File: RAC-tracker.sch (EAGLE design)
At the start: 26 parts, among them J1 U.FL, J2 U.FL, J5 CORTEX_JTAG_DEBUG_MINIMUM_SMD, U1 NRF9160-SICA-R, U2 SIM-ST-MFF2, U3 MCP73831, U4 SKY65723-81, U5 MIC5365-1.8YC5-TR

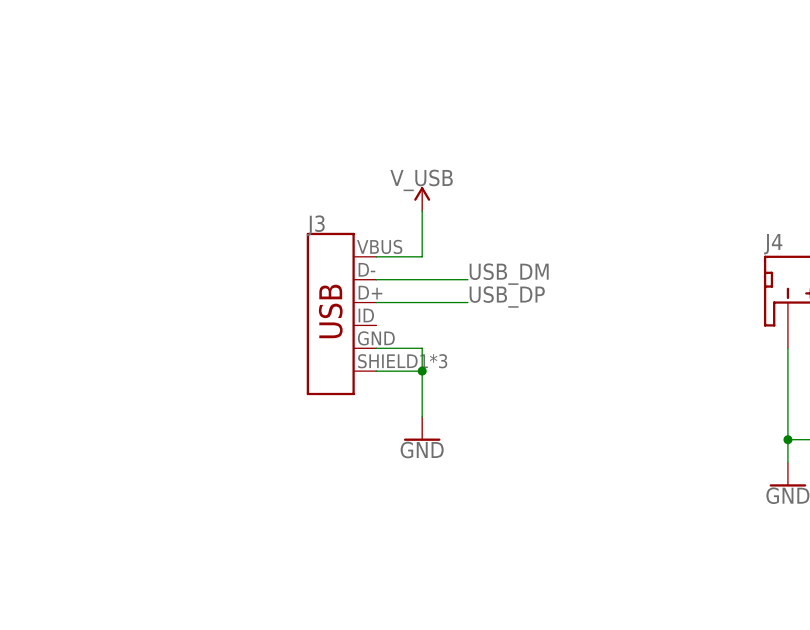
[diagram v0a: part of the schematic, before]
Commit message: Added a purchasable Molex Micro-USB connector
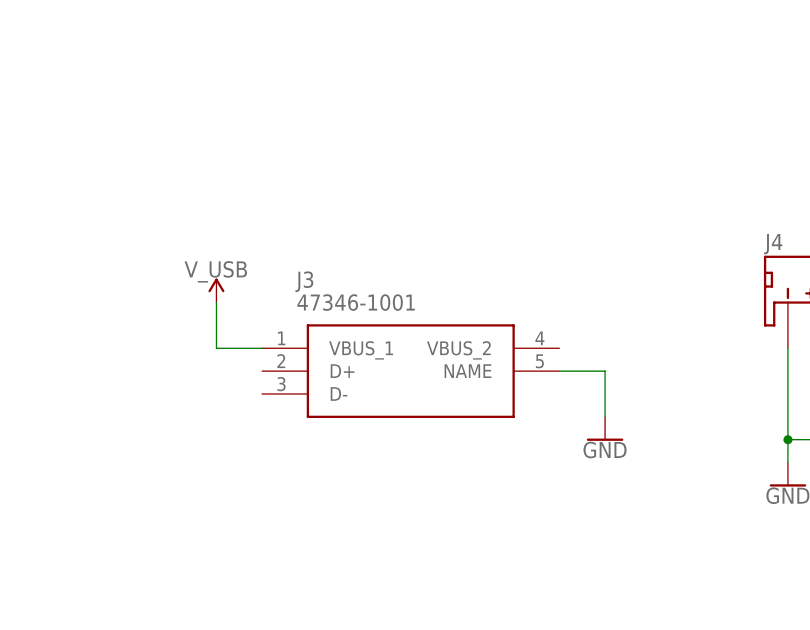
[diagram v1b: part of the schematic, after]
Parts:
- J3: value (none) -> 47346-1001; device SparkFun-Connectors:USB_MICRO-B_FEMALE-SMT -> rocket-components:47346-1001
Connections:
- removed net USB_DM: J3.D-
- removed net USB_DP: J3.D+
- net GND: now also J3.NAME; no longer J3.GND, J3.SHIELD
- net V_USB: now also J3.VBUS_1; no longer J3.VBUS
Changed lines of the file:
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@@
 <part name="C5" library="SparkFun-Capacitors" library_urn="urn:adsk.eagle:library:510" deviceset="0.1UF" device="-0603-25V-(+80/-20%)" package3d_urn="urn:adsk.eagle:package:37414/1" value="0.1uF"/>
 <part name="GND1" library="SparkFun-PowerSymbols" library_urn="urn:adsk.eagle:library:530" deviceset="GND" device=""/>
-<part name="J3" library="SparkFun-Connectors" deviceset="USB_MICRO-B" device="_FEMALE-SMT"/>
-<part name="SUPPLY4" library="SparkFun-PowerSymbols" library_urn="urn:adsk.eagle:library:530" deviceset="V_USB" device=""/>
-<part name="GND9" library="SparkFun-PowerSymbols" library_urn="urn:adsk.eagle:library:530" deviceset="GND" device=""/>
 <part name="U3" library="SparkFun-IC-Power" deviceset="MCP73831" device=""/>
 <part name="SUPPLY6" library="SparkFun-PowerSymbols" library_urn="urn:adsk.eagle:library:530" deviceset="V_USB" device=""/>
@@
 <part name="SUPPLY2" library="SparkFun-PowerSymbols" library_urn="urn:adsk.eagle:library:530" deviceset="1.8V" device=""/>
 <part name="GND19" library="SparkFun-PowerSymbols" library_urn="urn:adsk.eagle:library:530" deviceset="GND" device=""/>
+<part name="J3" library="rocket-components" deviceset="47346-1001" device=""/>
+<part name="SUPPLY3" library="SparkFun-PowerSymbols" library_urn="urn:adsk.eagle:library:530" deviceset="V_USB" device=""/>
+<part name="GND20" library="SparkFun-PowerSymbols" library_urn="urn:adsk.eagle:library:530" deviceset="GND" device=""/>
 </parts>
 <sheets>
@@
 <attribute name="VALUE" x="-20.32" y="-45.974" size="1.778" layer="96" align="top-center"/>
 </instance>
-<instance part="J3" gate="J1" x="165.1" y="12.7" smashed="yes">
-<attribute name="VALUE" x="162.56" y="2.794" size="1.778" layer="96" font="vector" rot="MR180" align="top-left"/>
-<attribute name="NAME" x="162.56" y="23.114" size="1.778" layer="95" font="vector"/>
-</instance>
-<instance part="SUPPLY4" gate="G$1" x="175.26" y="25.4" smashed="yes">
-<attribute name="VALUE" x="175.26" y="28.194" size="1.778" layer="96" align="bottom-center"/>
-</instance>
-<instance part="GND9" gate="1" x="175.26" y="0" smashed="yes">
-<attribute name="VALUE" x="175.26" y="-0.254" size="1.778" layer="96" align="top-center"/>
-</instance>
 <instance part="U3" gate="G$1" x="193.04" y="-38.1" smashed="yes">
 <attribute name="NAME" x="185.42" y="-32.512" size="1.778" layer="95"/>
@@
 <instance part="GND19" gate="1" x="-81.28" y="0" smashed="yes">
 <attribute name="VALUE" x="-81.28" y="-0.254" size="1.778" layer="96" align="top-center"/>
+</instance>
+<instance part="J3" gate="G$1" x="157.48" y="10.16" smashed="yes">
+<attribute name="NAME" x="161.29" y="17.78" size="1.778" layer="95" align="center-left"/>
+<attribute name="VALUE" x="161.29" y="15.24" size="1.778" layer="96" align="center-left"/>
+</instance>
+<instance part="SUPPLY3" gate="G$1" x="152.4" y="15.24" smashed="yes">
+<attribute name="VALUE" x="152.4" y="18.034" size="1.778" layer="96" align="bottom-center"/>
+</instance>
+<instance part="GND20" gate="1" x="195.58" y="0" smashed="yes">
+<attribute name="VALUE" x="195.58" y="-0.254" size="1.778" layer="96" align="top-center"/>
 </instance>
 </instances>
@@
 <wire x1="-25.4" y1="-35.56" x2="-20.32" y2="-35.56" width="0.1524" layer="91"/>
 <junction x="-20.32" y="-35.56"/>
-</segment>
-<segment>
-<pinref part="J3" gate="J1" pin="SHIELD"/>
-<wire x1="170.18" y1="7.62" x2="175.26" y2="7.62" width="0.1524" layer="91"/>
-<pinref part="GND9" gate="1" pin="GND"/>
-<wire x1="175.26" y1="7.62" x2="175.26" y2="2.54" width="0.1524" layer="91"/>
-<pinref part="J3" gate="J1" pin="GND"/>
-<wire x1="170.18" y1="10.16" x2="175.26" y2="10.16" width="0.1524" layer="91"/>
-<wire x1="175.26" y1="10.16" x2="175.26" y2="7.62" width="0.1524" layer="91"/>
-<junction x="175.26" y="7.62"/>
 </segment>
 <segment>
@@
 <wire x1="-81.28" y1="7.62" x2="-76.2" y2="7.62" width="0.1524" layer="91"/>
 </segment>
+<segment>
+<pinref part="J3" gate="G$1" pin="NAME"/>
+<wire x1="190.5" y1="7.62" x2="195.58" y2="7.62" width="0.1524" layer="91"/>
+<wire x1="195.58" y1="7.62" x2="195.58" y2="2.54" width="0.1524" layer="91"/>
+<pinref part="GND20" gate="1" pin="GND"/>
+</segment>
 </net>
 <net name="SIM_VIN" class="0">
@@
 <net name="V_USB" class="0">
 <segment>
-<pinref part="J3" gate="J1" pin="VBUS"/>
-<wire x1="170.18" y1="20.32" x2="175.26" y2="20.32" width="0.1524" layer="91"/>
-<pinref part="SUPPLY4" gate="G$1" pin="V_USB"/>
-<wire x1="175.26" y1="20.32" x2="175.26" y2="25.4" width="0.1524" layer="91"/>
-</segment>
-<segment>
 <pinref part="R2" gate="G$1" pin="2"/>
 <wire x1="167.64" y1="-40.64" x2="167.64" y2="-35.56" width="0.1524" layer="91"/>
@@
 <junction x="157.48" y="-35.56"/>
 </segment>
-</net>
-<net name="USB_DM" class="0">
-<segment>
-<pinref part="J3" gate="J1" pin="D-"/>
-<wire x1="170.18" y1="17.78" x2="180.34" y2="17.78" width="0.1524" layer="91"/>
-<label x="180.34" y="17.78" size="1.778" layer="95"/>
-</segment>
-</net>
-<net name="USB_DP" class="0">
-<segment>
-<pinref part="J3" gate="J1" pin="D+"/>
-<wire x1="170.18" y1="15.24" x2="180.34" y2="15.24" width="0.1524" layer="91"/>
-<label x="180.34" y="15.24" size="1.778" layer="95"/>
-</segment>
-</net>
+<segment>
+<pinref part="J3" gate="G$1" pin="VBUS_1"/>
+<wire x1="157.48" y1="10.16" x2="152.4" y2="10.16" width="0.1524" layer="91"/>
+<wire x1="152.4" y1="10.16" x2="152.4" y2="15.24" width="0.1524" layer="91"/>
+<pinref part="SUPPLY3" gate="G$1" pin="V_USB"/>
+</segment>
+</net>

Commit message: U.FL replaced to fit BOM, polygons adjusted. Fab ready!
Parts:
- C1: value 4.7uF -> 56pF; device SparkFun-Capacitors:4.7UF0603 -> rocket-components:GRM1885C1H560JA01J
- C10: value 1.0uF -> 47uF; device SparkFun-Capacitors:1.0UF-0603-16V-10% -> rocket-components:JMK212BBJ476MG-T
- C2: value 4.7uF -> 0.1uF; device SparkFun-Capacitors:4.7UF0603 -> SparkFun-Capacitors:0.1UF-0603-25V-(+80/-20%)
- C3: value 4.7uF -> 1.0uF; device SparkFun-Capacitors:4.7UF0603 -> SparkFun-Capacitors:1.0UF-0603-16V-10%
- C4: value 47uF -> 1.0uF; device rocket-components:JMK212BBJ476MG-T -> SparkFun-Capacitors:1.0UF-0603-16V-10%
- C5: value 0.1uF -> 4.7uF; device SparkFun-Capacitors:0.1UF-0603-25V-(+80/-20%) -> SparkFun-Capacitors:4.7UF0603
- C8: value 56pF -> 4.7uF; device rocket-components:GRM1885C1H560JA01J -> SparkFun-Capacitors:4.7UF0603
- C9: value 1.0uF -> 4.7uF; device SparkFun-Capacitors:1.0UF-0603-16V-10% -> SparkFun-Capacitors:4.7UF0603
- J1, J2: value U.FL -> 2337019-1; device SparkFun-Connectors:U.FL -> rocket-components:2337019-1
- R1: value 2.0k -> 1k; device SparkFun-Resistors:2.0KOHM-0603-1/10W-5% -> SparkFun-Resistors:1KOHM-0603-1/10W-1%
- R2: value 1k -> 2.0k; device SparkFun-Resistors:1KOHM-0603-1/10W-1% -> SparkFun-Resistors:2.0KOHM-0603-1/10W-5%
- renumbered D3 to D2
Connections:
- net 1.8V: now also C1.1, C4.1, C7.1; no longer C10.1, C3.1, C8.1
- net GND: now also J1.GND_1, J1.GND_2, J2.GND_1, J2.GND_2, R2.1; no longer J1.GND@0, J1.GND@1, J2.GND@0, J2.GND@1, R1.1
- net IO_SUP: now also C10.1; no longer C4.1
- net PROG: now also R2.2; no longer R1.2
- net SIM_VIN: now also C2.1; no longer C5.1
- net STAT_AN: now also R1.1; no longer R2.1
- net V_BATT: now also C3.1, C5.1, C6.1; no longer C1.1, C2.1, C7.1
- net V_USB: now also C8.1, R1.2; no longer C6.1, R2.2
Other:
- moved on the sheet: C2, C3, C5, C6, C7, C9, R1, R2

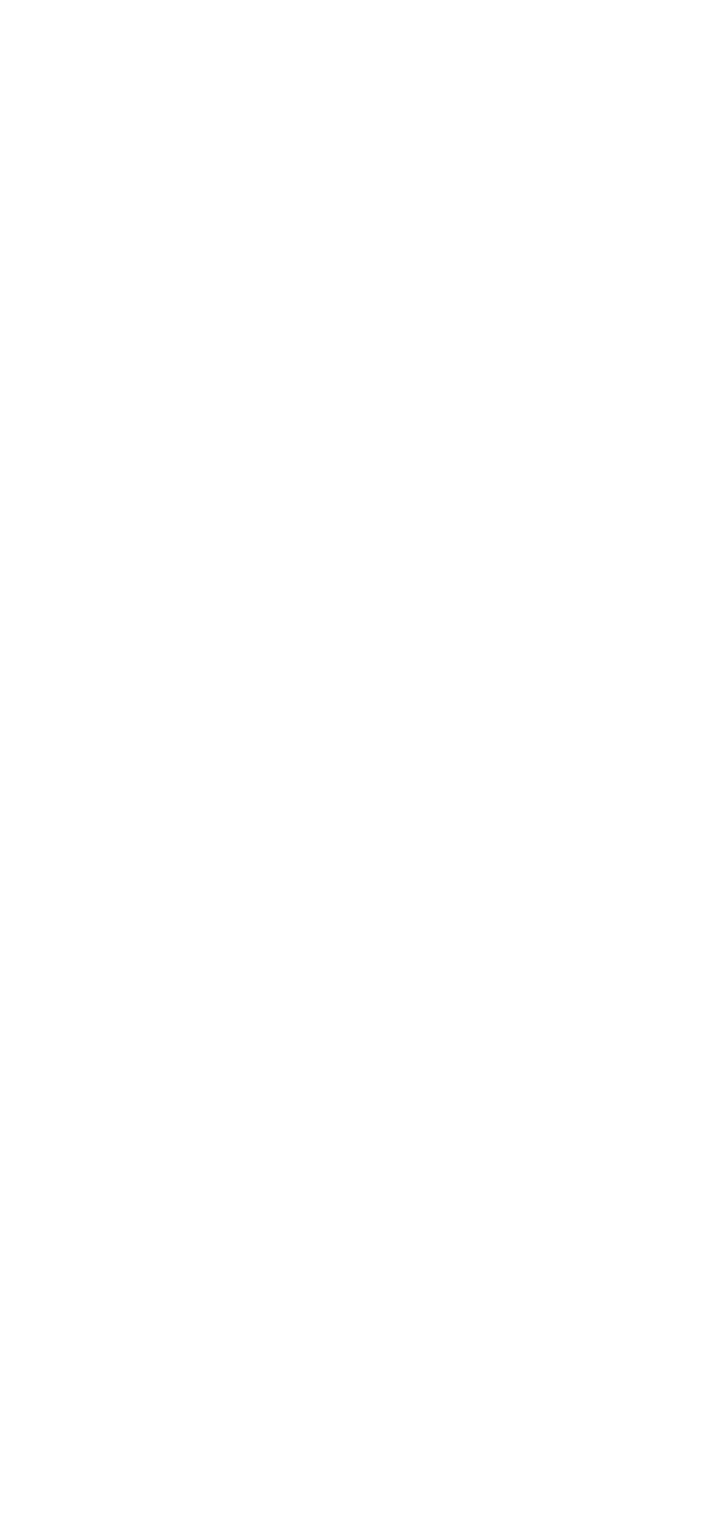
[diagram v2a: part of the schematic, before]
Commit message: Starting again with the SIM7000
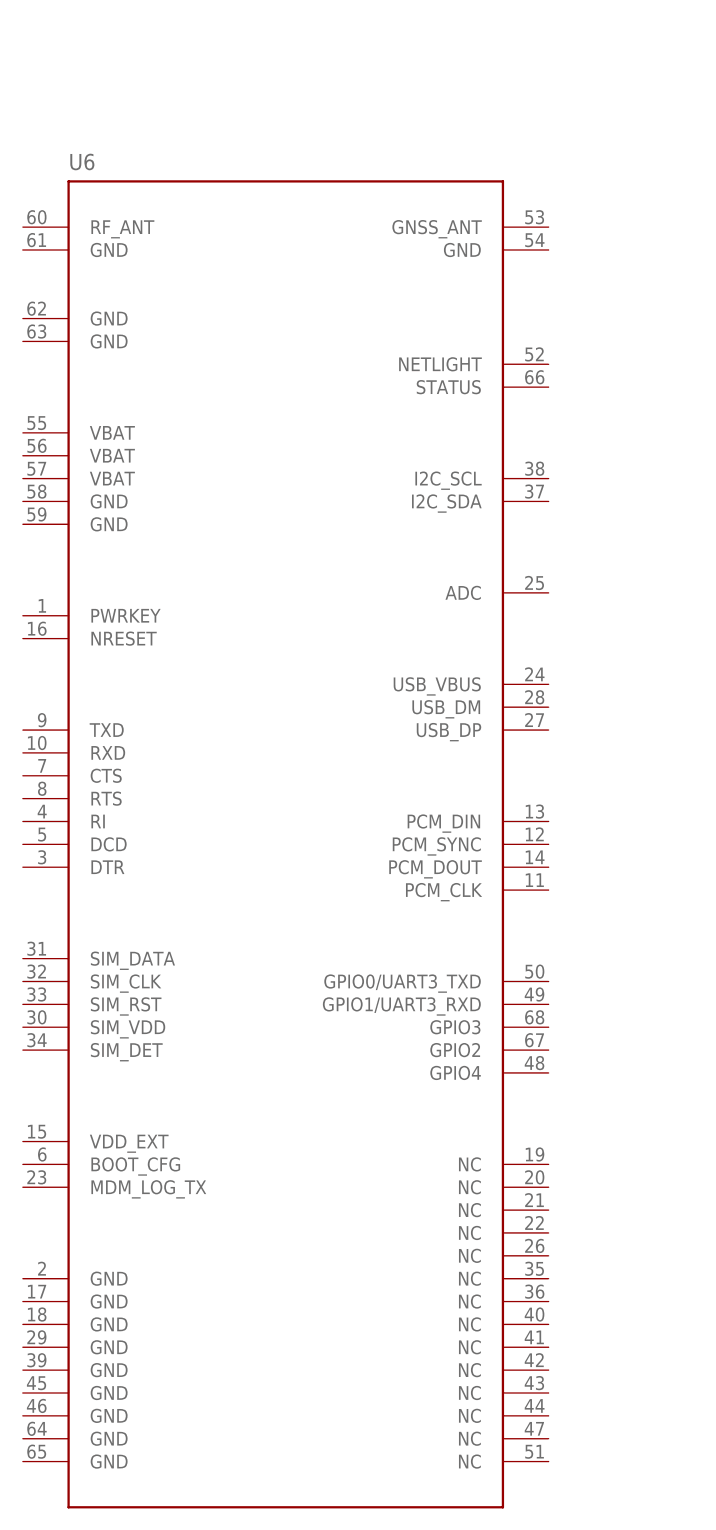
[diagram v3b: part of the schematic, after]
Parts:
- added U6: (no value), rocket-components:SIM7000
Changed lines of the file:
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@@
 <part name="GND9" library="SparkFun-PowerSymbols" library_urn="urn:adsk.eagle:library:530" deviceset="GND" device=""/>
 <part name="GND21" library="SparkFun-PowerSymbols" library_urn="urn:adsk.eagle:library:530" deviceset="GND" device=""/>
+<part name="U6" library="rocket-components" deviceset="SIM7000" device=""/>
 </parts>
 <sheets>
@@
 <attribute name="VALUE" x="-71.12" y="45.466" size="1.778" layer="96" align="top-center"/>
 </instance>
+<instance part="U6" gate="G$1" x="-200.66" y="-60.96" smashed="yes">
+<attribute name="NAME" x="-200.66" y="87.63" size="1.778" layer="95"/>
+<attribute name="VALUE" x="-185.42" y="43.18" size="3.81" layer="96"/>
+</instance>
 </instances>

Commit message: Set up minimum schematic for SIM7000
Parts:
- removed C10: 47uF, rocket-components:JMK212BBJ476MG-T
- removed C3, C4: 1.0uF, SparkFun-Capacitors:1.0UF-0603-16V-10%
- removed C5, C6, C7: 4.7uF, SparkFun-Capacitors:4.7UF0603
- removed J5: CORTEX_JTAG_DEBUG_MINIMUM_SMD, SparkFun-Connectors:CORTEX_JTAG_DEBUG_MINIMUM_SMD
- removed R3: 10k, SparkFun-Resistors:10KOHM-0603-1/10W-1%
- removed R4: 1M, SparkFun-Resistors:1MOHM-0603-1/4W-5%
- removed U1: NRF9160-SICA-R, rocket-components:NRF9160-SICA-R
- removed U5: MIC5365-1.8YC5-TR, rocket-components:MIC5365-1.8YC5-TR
- added C11: 0.1uF, SparkFun-Capacitors:0.1UF-0603-25V-(+80/-20%)
- added C12: 1.0uF, SparkFun-Capacitors:1.0UF-0603-16V-10%
- added C13, C14, C15: 100uF, rocket-components:JMK316ABJ107ML-T
- added D3, D4: 250mA/100V, SparkFun-DiscreteSemi:DIODE-BAS16J
- added FB1: 30Ω/1.8A, SparkFun-Coils:FERRITE_BEAD-0603
- added S1: MOMENTARY-SWITCH-SPST-SMD-5.2MM, SparkFun-Switches:MOMENTARY-SWITCH-SPST-SMD-5.2MM
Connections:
- removed net !RST: J5.!RESET, U1.NRESET
- removed net EN: R3.1, U1.ENABLE
- removed net GPS_EN: R4.2, U1.MAGPIO0, U4.VEN
- removed net IO_SUP: C10.1, U1.IO_SUPPLY
- removed net SWDCLK: J5.SWDCLK, U1.SWDCLK
- removed net SWDIO: J5.SWDIO, U1.SWDIO
- new net !LTE_RST: D4.C
- new net DTR: U6.DTR
- new net LTE_PWR: D3.C, S1.2
- new net NRESET: D4.A, U6.NRESET
- new net PWRKEY: D3.A, U6.PWRKEY
- new net RI: U6.RI
- new net RXD: U6.RXD
- new net TXD: U6.TXD
- new net USB_DM: J3.D-, U6.USB_DM
- new net USB_DP: J3.D+, U6.USB_DP
- new net VCC: C11.1, C12.1, C13.1, C14.1, C15.1, FB1.2, U6.VBAT, U6.VBAT@1, U6.VBAT@2
- net 1.8V: now also U4.VEN, U6.VDD_EXT; no longer C4.1, C7.1, J5.VCC, U1.VDD_GPIO, U5.VOUT
- net GND: now also C11.2, C12.2, C13.2, C14.2, C15.2, S1.1, U6.GND, U6.GND@1, U6.GND@10, U6.GND@11, U6.GND@12, U6.GND@13, U6.GND@14, U6.GND@2, U6.GND@3, U6.GND@4, U6.GND@5, U6.GND@6, U6.GND@7, U6.GND@8, U6.GND@9; no longer C10.2, C3.2, C4.2, C5.2, C6.2, C7.2, J5.GND, R4.1, U1.GND_SHIELD, U1.VSS, U5.GND
- net GPS_RF: now also U6.GNSS_ANT; no longer U1.GPS
- net LTE_ANT: now also U6.RF_ANT; no longer U1.ANT
- net SIM_CLK: now also U6.SIM_CLK; no longer U1.SIM_CLK
- net SIM_DATA: now also U6.SIM_DATA; no longer U1.SIM_IO
- net SIM_RST: now also U6.SIM_RST; no longer U1.SIM_RST
- net SIM_VIN: now also U6.SIM_VDD; no longer U1.SIM_1V8
- net V_BATT: now also FB1.1; no longer C3.1, C5.1, C6.1, R3.2, U1.VDD, U5.EN, U5.VIN
- net V_USB: now also U6.USB_VBUS
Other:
- moved on the sheet: C2, J1, J2, U2, U6

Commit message: Replaced u.FL connectors with SMD antennas
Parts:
- removed J1, J2: 2337019-1, rocket-components:2337019-1
- removed S1: MOMENTARY-SWITCH-SPST-SMD-5.2MM, SparkFun-Switches:MOMENTARY-SWITCH-SPST-SMD-5.2MM
- added AE1: FR01-S4-232L, rocket-components:FR01-S4-232L
- added AE2: W3011, rocket-components:W3011
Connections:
- net USB_DM renamed USB_N
- net USB_DP renamed USB_P
- net GND: now also AE2.GND; no longer J1.GND_1, J1.GND_2, J2.GND_1, J2.GND_2, S1.1
- net GPS_ANT: now also AE2.FEED; no longer J1.SIGNAL
- net LTE_ANT: now also AE1.SIGNAL; no longer J2.SIGNAL
- net LTE_PWR: no longer S1.2
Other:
- moved on the sheet: C1, C2, C8, C9, D1, D2, J3, J4, R1, R2, U2, U3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

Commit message: Added ATMEGA328P and BMP388 to schematic, likely won't keep
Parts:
- removed D3, D4: 250mA/100V, SparkFun-DiscreteSemi:DIODE-BAS16J
- added C3, C5: 0.1uF, SparkFun-Capacitors:0.1UF-0603-25V-(+80/-20%)
- added C4: 4.7uF, SparkFun-Capacitors:4.7UF0603
- added D5: BLUE, SparkFun-LED:LED-BLUE0603
- added D6: GREEN, SparkFun-LED:LED-GREEN0603
- added JP1: (no value), pinhead:PINHD-1X6
- added Q1, Q2: 220mA/50V/3.5Ω, SparkFun-DiscreteSemi:MOSFET-NCH-BSS138
- added R3: 2.0k, SparkFun-Resistors:2.0KOHM-0603-1/10W-5%
- added R4: 470, SparkFun-Resistors:470OHM-0603-1/10W-1%
- added R5, R6: 4.7k, SparkFun-Resistors:4.7KOHM-0603-1/10W-1%
- added U1: ATMEGA328P, SparkFun-IC-Microcontroller:ATMEGA328P_VQFNVQFN
- added U5: BMP388, SparkFun-Sensors:BMP388BMP388
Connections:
- removed net !LTE_RST: D4.C
- removed net LTE_PWR: D3.C
- removed net RXD: U6.RXD
- removed net TXD: U6.TXD
- new net LED_NET_A: D5.A, R4.1
- new net LED_NET_C: D5.C, Q2.D
- new net LED_STAT_A: D6.A, R3.1
- new net LED_STAT_C: D6.C, Q1.D
- new net LTE_RXD: U1.PD1(TXD), U6.RXD
- new net LTE_TXD: U1.PD0(RXD), U6.TXD
- new net MCU_RST: JP1.3, U1.PC6(/RESET)
- new net MISO: JP1.5, U1.PB4(MISO)
- new net MOSI: JP1.4, U1.PB3(MOSI/OC2)
- new net NETLIGHT: Q2.G, U6.NETLIGHT
- new net SCK: JP1.6, U1.PB5(SCK)
- new net SCL: R6.1, U1.PC5(ADC5/SCL), U5.SCK
- new net SDA: R5.1, U1.PC4(ADC4/SDA), U5.SDI/SDA
- new net STATUS: Q1.G, U6.STATUS
- net 1.8V: now also C5.1, R5.2, R6.2, U5.CS, U5.VDD
- net DTR: now also U1.PD3(INT1)
- net GND: now also C3.2, C4.2, C5.2, JP1.2, Q1.S, Q2.S, U1.GND, U1.GND@PAD, U5.GND
- net NRESET: now also U1.PC1(ADC1); no longer D4.A
- net PWRKEY: now also U1.PC0(ADC0); no longer D3.A
- net RI: now also U1.PD2(INT0)
- net V_BATT: now also C3.1, C4.1, JP1.1, R3.2, R4.2, U1.AREF, U1.AVCC, U1.VCC
